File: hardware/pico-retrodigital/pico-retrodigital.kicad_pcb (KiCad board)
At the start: 2 copper layers, 53.8 x 35 mm, 44 parts, among them J1 Conn_02x05_Top_Bottom, J2 HDMI_A, J4 Conn_01x02_Pin, J5 USB_C, J5 USB_C_Plug_USB2.0, SW1 SW_Push, U6 74LVC2G17, U7 RP2350B, U8 NCP1117-3.3_SOT223, Y1 ABM8-272-T3

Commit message: PCB fixes
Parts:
- removed C4: 0.1u, Capacitor_SMD:C_0603_1608Metric
- removed J2: HDMI_A, Connector_Video:HDMI_A_Molex_208658-1001_Horizontal
- removed the J5 at (72.5, 107.2)
- removed the J5 at (73.8, 123.2)
- added C14: 4.7u, Capacitor_SMD:C_0402_1005Metric, F.Cu at (23.3, 120.6)
- added C15: 4.7u, Capacitor_SMD:C_0402_1005Metric, F.Cu at (23.3, 122.5)
- added J3: Conn_01x14, Connector_FFC-FPC:TE_1-1734839-4_1x14-1MP_P0.5mm_Horizontal, F.Cu at (95.3, 92.5)
- added J5: USB_C_Plug_USB2.0, pico-retrodigital:USB_C_Receptacle_Jing_918-418K2023S40001, F.Cu at (73.1, 105.1)
- added L1: 3.3u, Inductor_SMD:L_0805_2012Metric, F.Cu at (29.7, 120.6)
- U7: value RP2350B -> RP2354B; footprint rpi-lib-kicad-rp235x:QFN-80-1EP_10x10mm_P0.4mm_EP3.4x3.4mm_ThermalVias -> Package_DFN_QFN:QFN-80-1EP_10x10mm_P0.4mm_EP3.4x3.4mm_ThermalVias
- moved C13 47.2 mm to (23.3, 118.6)
- moved R15 46.9 mm to (37.5, 119.0)
- moved R14 38.5 mm to (37.5, 117.0), turned to 0 degrees
- moved R13 36.8 mm to (37.5, 115.0), turned to 0 degrees
- moved SW1 31.9 mm to (25.2, 91.9)
- moved R11 22.5 mm to (37.5, 113.0)
- moved D3 19.7 mm to (35.5, 109.5)
- moved D1 10.9 mm to (29.5, 123.2)
- moved J4 10.7 mm to (29.7, 114.3), turned to 0 degrees
- moved R16 9.94 mm to (34.0, 118.3)
- moved R17 9.94 mm to (34.0, 120.8)
- moved R18 9.94 mm to (34.0, 123.3)
- moved C7 7.95 mm to (23.7, 114.8), turned to 0 degrees
- moved F1 4.08 mm to (34.0, 113.3), turned to 0 degrees
- moved FB1 1.22 mm to (34.0, 115.8)
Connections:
- C12 pad 1: VBUS -> 5V
- D3 pad 1: VBUS -> 5V
- U7 pad 10: Net-(U7-DVDD-Pad10) -> unconnected-(U7-DVDD-Pad10)
- U7 pad 15: Net-(U7-IOVDD-Pad15) -> unconnected-(U7-IOVDD-Pad15)_6
- U7 pad 20: unconnected-(U7-GPIO20-Pad20) -> SDA
- U7 pad 21: unconnected-(U7-GPIO21-Pad21) -> SCL
- U7 pad 22: CTL_0 -> CEC_PICO
- U7 pad 23: CTL_1 -> unconnected-(U7-GPIO23-Pad23)
- U7 pad 24: Net-(U7-IOVDD-Pad15) -> unconnected-(U7-IOVDD-Pad15)_7
- U7 pad 25: CTL_2 -> CTL_0
- U7 pad 26: CTL_3 -> CTL_1
- U7 pad 27: CTL_4 -> CTL_2
- U7 pad 28: CTL_5 -> CTL_3
- U7 pad 29: Net-(U7-IOVDD-Pad15) -> unconnected-(U7-IOVDD-Pad15)
- U7 pad 32: Net-(U7-DVDD-Pad10) -> unconnected-(U7-DVDD-Pad10)_2
- U7 pad 41: Net-(U7-IOVDD-Pad15) -> unconnected-(U7-IOVDD-Pad15)_1
- U7 pad 5: Net-(U7-IOVDD-Pad15) -> unconnected-(U7-IOVDD-Pad15)_2
- U7 pad 50: Net-(U7-IOVDD-Pad15) -> unconnected-(U7-IOVDD-Pad15)_4
- U7 pad 51: Net-(U7-DVDD-Pad10) -> unconnected-(U7-DVDD-Pad10)_1
- U7 pad 60: Net-(U7-IOVDD-Pad15) -> unconnected-(U7-IOVDD-Pad15)_3
- U7 pad 76: Net-(U7-IOVDD-Pad15) -> unconnected-(U7-IOVDD-Pad15)_5
- U7 pad 77: unconnected-(U7-GPIO0-Pad77) -> AUD_DAT
- U7 pad 78: unconnected-(U7-GPIO1-Pad78) -> AUD_WS
- U7 pad 79: unconnected-(U7-GPIO2-Pad79) -> AUD_CLK
- U7 pad 8: unconnected-(U7-GPIO10-Pad8) -> AUX_A
- U7 pad 9: unconnected-(U7-GPIO11-Pad9) -> AUX_B
- U8 pad 3: VBUS -> 5V
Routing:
- net 5V: track 11.1 -> 0.00 mm
- net USB_D-: track 3.73 -> 0.00 mm
- net USB_D+: track 3.72 -> 0.00 mm
- net Net-(F1-Pad1): track 1.61 -> 0.00 mm
- net Net-(D1-K): track 1.61 -> 0.00 mm

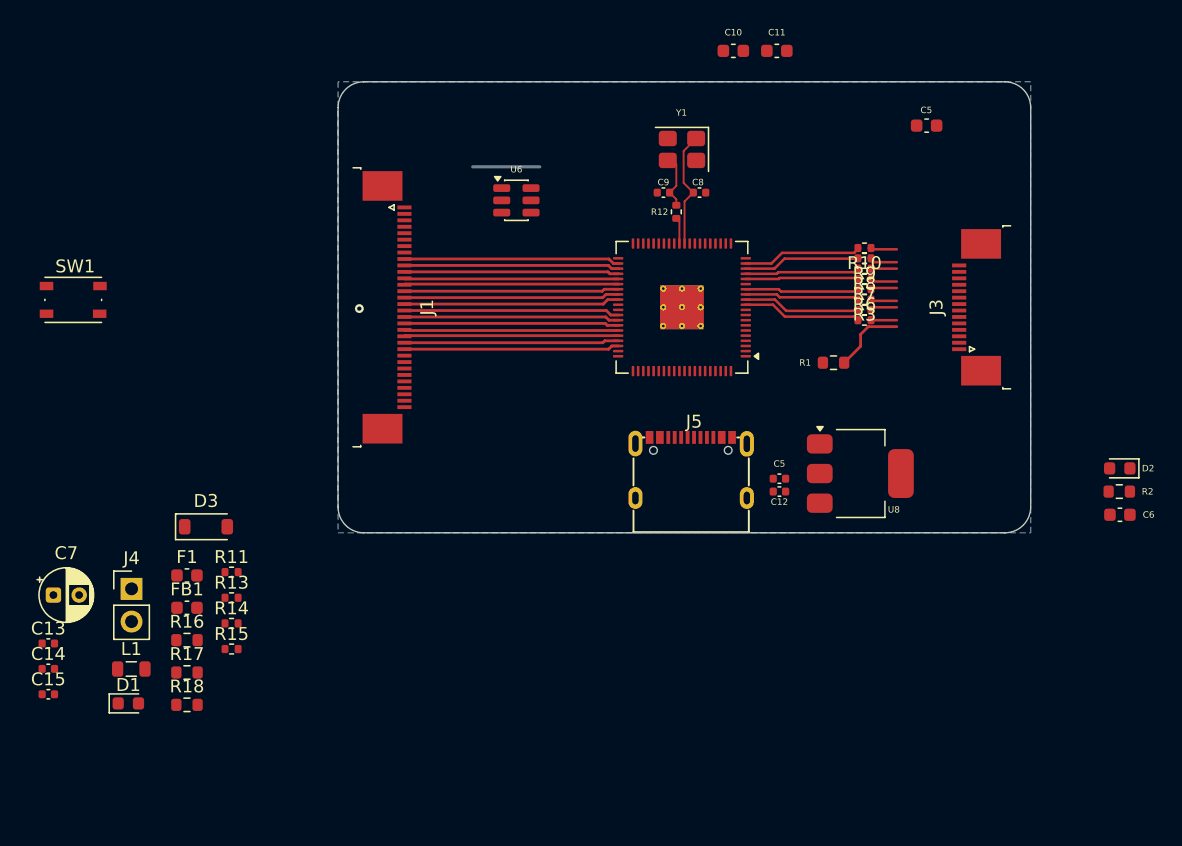
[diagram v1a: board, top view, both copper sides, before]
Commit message: Square-shaped PCB
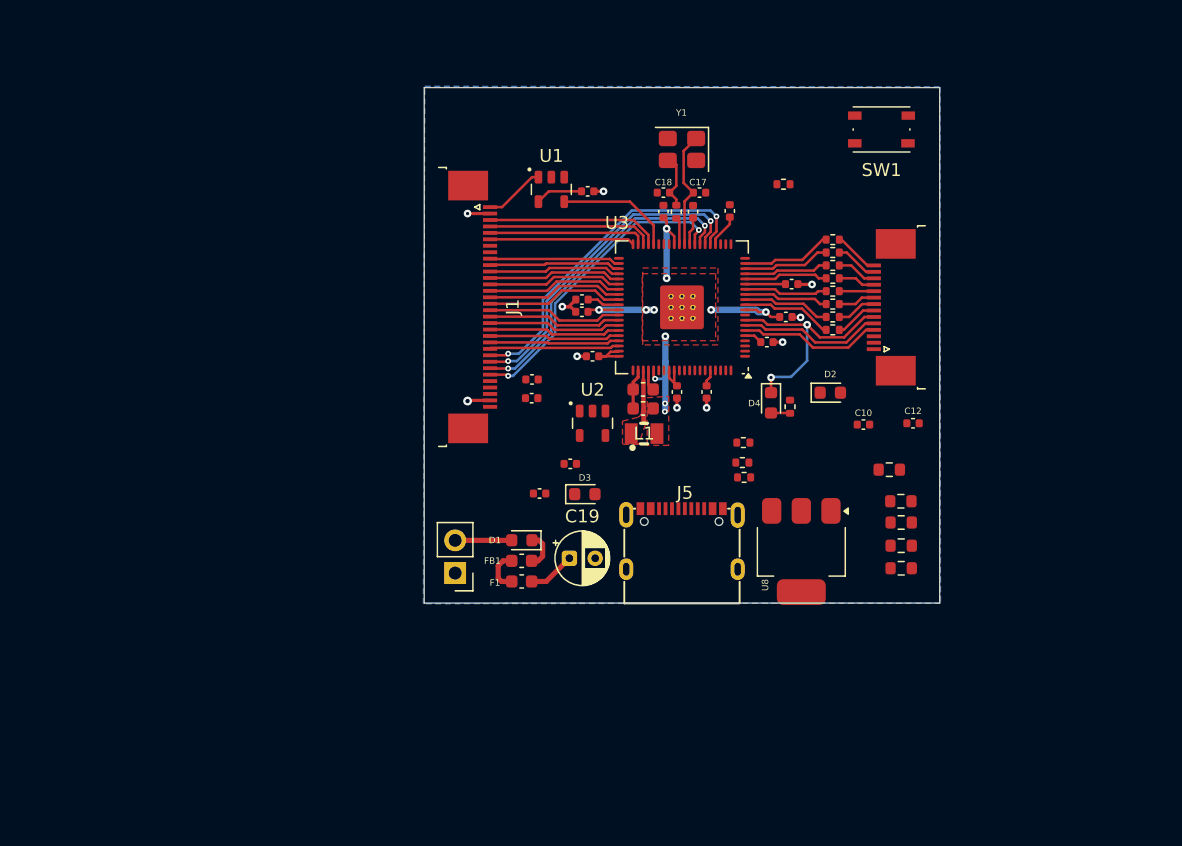
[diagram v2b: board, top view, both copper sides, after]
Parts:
- removed the C10 at (76.4, 72.6)
- removed the C5 at (91.4, 78.4)
- removed U6: 74LVC2G17, Package_TO_SOT_SMD:SOT-23-6
- added C1: 0.1u, Capacitor_SMD:C_0402_1005Metric, F.Cu at (81.0, 90.7)
- added C16: 0.1u, Capacitor_SMD:C_0402_1005Metric, F.Cu at (65.1, 83.5)
- added C19: 47u, Capacitor_THT:CP_Radial_D4.0mm_P2.00mm, F.Cu at (63.7, 112.0)
- added C2: 0.1u, Capacitor_SMD:C_0603_1608Metric, F.Cu at (69.4, 98.9)
- added C20: 0.1u, Capacitor_SMD:C_0402_1005Metric, F.Cu at (64.7, 92.8)
- added C21: 0.1u, Capacitor_SMD:C_0402_1005Metric, F.Cu at (71.0, 85.1)
- added C22: 0.1u, Capacitor_SMD:C_0402_1005Metric, F.Cu at (80.5, 93.2)
- added C3: 0.1u, Capacitor_SMD:C_0402_1005Metric, F.Cu at (64.7, 91.9)
- added C4: 0.1u, Capacitor_SMD:C_0402_1005Metric, F.Cu at (65.5, 96.3)
- added C5: 0.1u, Capacitor_SMD:C_0402_1005Metric, F.Cu at (76.2, 85.0)
- added C5: 0.1u, Capacitor_SMD:C_0402_1005Metric, F.Cu at (73.3, 85.1)
- added C8: 0.1u, Capacitor_SMD:C_0402_1005Metric, F.Cu at (72.0, 99.1)
- added C9: 0.1u, Capacitor_SMD:C_0402_1005Metric, F.Cu at (60.8, 98.1)
- added D4: SS14, Diode_SMD:D_0603_1608Metric, F.Cu at (79.3, 99.9)
- added R19: 5.1k, Resistor_SMD:R_0603_1608Metric, F.Cu at (89.5, 112.8)
- added U1: SN74LVC1G17DBVR, pico-retrodigital:SOT-23-5, F.Cu at (62.3, 83.3)
- added U2: SN74LVC1G17DBVR, pico-retrodigital:SOT-23-5, F.Cu at (65.5, 101.5)
- C11, C6: footprint Capacitor_SMD:C_0603_1608Metric -> Capacitor_SMD:C_0402_1005Metric
- C14: footprint Capacitor_SMD:C_0402_1005Metric -> Capacitor_SMD:C_0603_1608Metric
- C7: value 47u -> 0.1u; footprint Capacitor_THT:CP_Radial_D4.0mm_P2.00mm -> Capacitor_SMD:C_0402_1005Metric
- D3: value D_Schottky -> SS14; footprint Diode_SMD:D_SOD-123 -> Diode_SMD:D_0603_1608Metric
- L1: value 3.3u -> ~; footprint Inductor_SMD:L_0805_2012Metric -> pico-retrodigital:IND-SMD_L2.0-W1.6_AOTA-B201610S3R3-101-T
- R1: footprint Resistor_SMD:R_0603_1608Metric -> Resistor_SMD:R_0402_1005Metric
- U3: renamed from U7; footprint Package_DFN_QFN:QFN-80-1EP_10x10mm_P0.4mm_EP3.4x3.4mm_ThermalVias -> rpi-lib-kicad-rp235x:QFN-80-1EP_10x10mm_P0.4mm_EP3.4x3.4mm_ThermalVias
- moved SW1 64.1 mm to (87.9, 78.7)
- moved R18 56.8 mm to (89.5, 111.0)
- moved R17 56.6 mm to (89.5, 109.2)
- moved R16 56.4 mm to (89.4, 107.5)
- moved C7 53.1 mm to (74.3, 99.1), turned to -90 degrees
- moved R11 52.3 mm to (80.3, 83.0)
- moved C14 50.4 mm to (69.4, 100.3)
- moved L1 43.8 mm to (69.5, 102.3), turned to 180 degrees
- moved C13 42.1 mm to (60.8, 99.5)
- moved R15 41.9 mm to (77.3, 105.7)
- moved R14 41.6 mm to (77.1, 104.5)
- moved R13 41.5 mm to (77.2, 103.0)
- moved C15 41.2 mm to (61.4, 107.0)
- moved C11 35.8 mm to (63.8, 104.7), turned to 180 degrees
- moved D1 33.1 mm to (60.0, 110.6), turned to 180 degrees
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- renumbered C5 to C10, C8 to C17, C9 to C18
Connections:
- C11 pad 1: 3V3 -> +3V3
- C12 pad 1: 5V -> +5V
- C6 pad 1: Net-(D2-K) -> +3V3
- C7 pad 1: 5V -> +3V3
- D1 pad 2: 5V -> +5V
- D2 pad 2: 5V -> +5V
- D3 pad 1: 5V -> +5V
- F1 pad 2: 5V -> +5V
- J4 pad 2: 5V -> +5V
- J5 pad B5: Net-(J5-CC1) -> Net-(J5-CC2)
- R1 pad 2: CEC_PICO -> Net-(D4-A)
- R2 pad 1: 5V -> +5V
- U3 pad 10: unconnected-(U7-DVDD-Pad10) -> +1V1
- U3 pad 15: unconnected-(U7-IOVDD-Pad15)_6 -> +3V3
- U3 pad 20: SDA -> AUX_B
- U3 pad 21: SCL -> AUX_A
- U3 pad 22: CEC_PICO -> unconnected-(U3-GPIO22-Pad22)
- U3 pad 24: unconnected-(U7-IOVDD-Pad15)_7 -> +3V3
- U3 pad 29: unconnected-(U7-IOVDD-Pad15) -> +3V3
- U3 pad 32: unconnected-(U7-DVDD-Pad10)_2 -> +1V1
- U3 pad 41: unconnected-(U7-IOVDD-Pad15)_1 -> +3V3
- U3 pad 5: unconnected-(U7-IOVDD-Pad15)_2 -> +3V3
- U3 pad 50: unconnected-(U7-IOVDD-Pad15)_4 -> +3V3
- U3 pad 51: unconnected-(U7-DVDD-Pad10)_1 -> +1V1
- U3 pad 59: unconnected-(U7-ADC_AVDD-Pad59) -> +3V3
- U3 pad 6: unconnected-(U7-GPIO8-Pad6) -> SDA
- U3 pad 60: unconnected-(U7-IOVDD-Pad15)_3 -> +3V3
- U3 pad 68: unconnected-(U7-USB_OTP_VDD-Pad68) -> +3V3
- U3 pad 69: unconnected-(U7-QSPI_IOVDD-Pad69) -> +3V3
- U3 pad 7: unconnected-(U7-GPIO9-Pad7) -> SCL
- U3 pad 76: unconnected-(U7-IOVDD-Pad15)_5 -> +3V3
- U3 pad 8: AUX_A -> CEC_PICO
- U3 pad 9: AUX_B -> unconnected-(U3-GPIO11-Pad9)
- U8 pad 3: 5V -> +5V
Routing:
- net +1V1: track 0.00 -> 28.8 mm, vias 0 -> 11
- net CTL_0: track 0.00 -> 26.1 mm, vias 0 -> 2
- net CTL_1: track 0.00 -> 25.4 mm, vias 0 -> 2
- net CTL_2: track 0.00 -> 24.7 mm, vias 0 -> 2
- net +3V3: track 0.00 -> 24.3 mm
- net CTL_3: track 0.00 -> 23.8 mm, vias 0 -> 2
- net CMOD_0: track 0.00 -> 13.5 mm
- net CMOD_1: track 0.00 -> 12.9 mm
- net CEC_PICO: track 5.79 -> 18.5 mm, vias 0 -> 2
- net CMOD_2: track 0.00 -> 12.2 mm
- net CMOD_3: track 0.00 -> 11.2 mm
- net SCL: track 0.00 -> 11.2 mm
- net SDA: track 0.00 -> 11.1 mm
- net GND: track 5.20 -> 14.6 mm, vias 1 -> 10
- net PCLK: track 0.00 -> 9.16 mm
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- added copper zone on F.Cu, net +1V1
- added copper zone on F.Cu, net Net-(U3-VREG_LX)
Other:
- board size 53.8 x 35 mm -> 40 x 40 mm

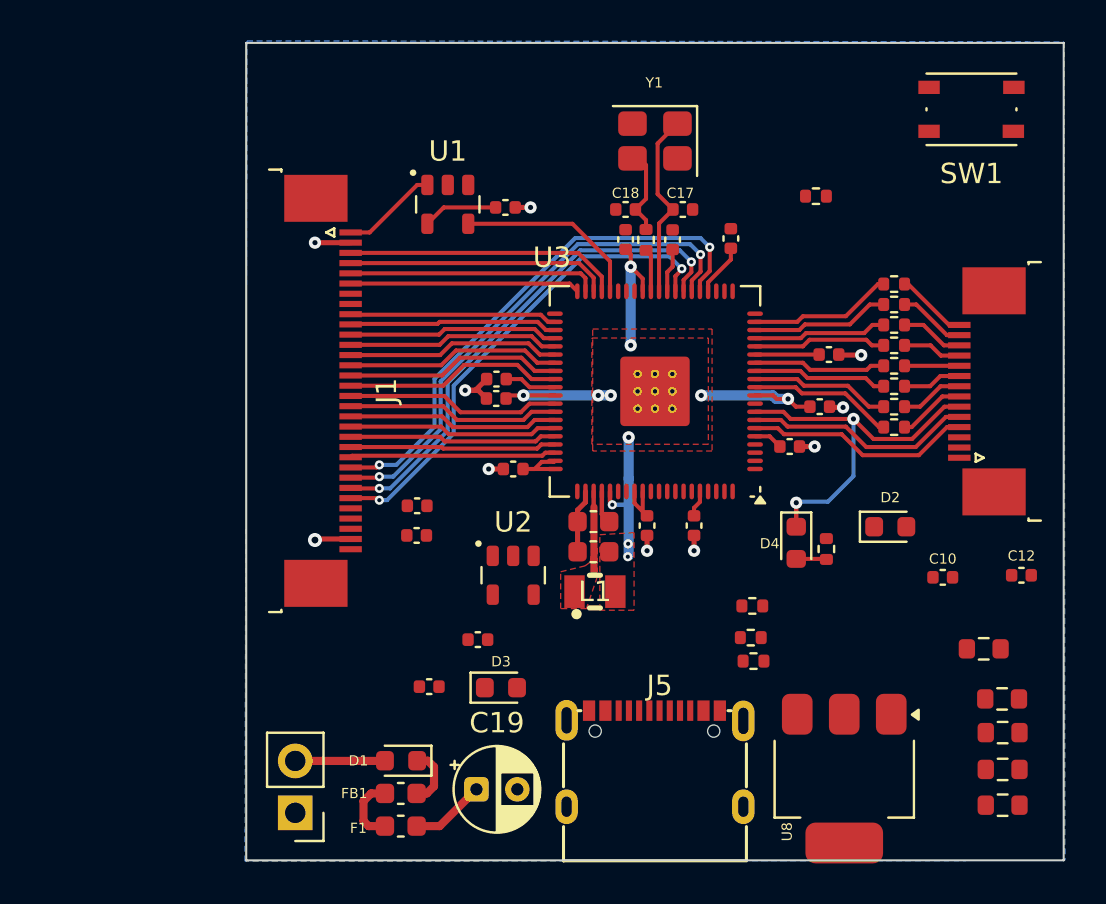
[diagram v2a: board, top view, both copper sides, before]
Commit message: Add 3V3 LDO regulator, reset/boot buttons, and pad default tweaks
- Add ME6217C33M5G LDO symbol and integrate into schematic
- Add RES1 (reset) and BOOT1 (boot) push buttons
- Update default pad size in board setup
- Ignore kicad-jlcpcb-tools plugin local state (jlcpcb/)
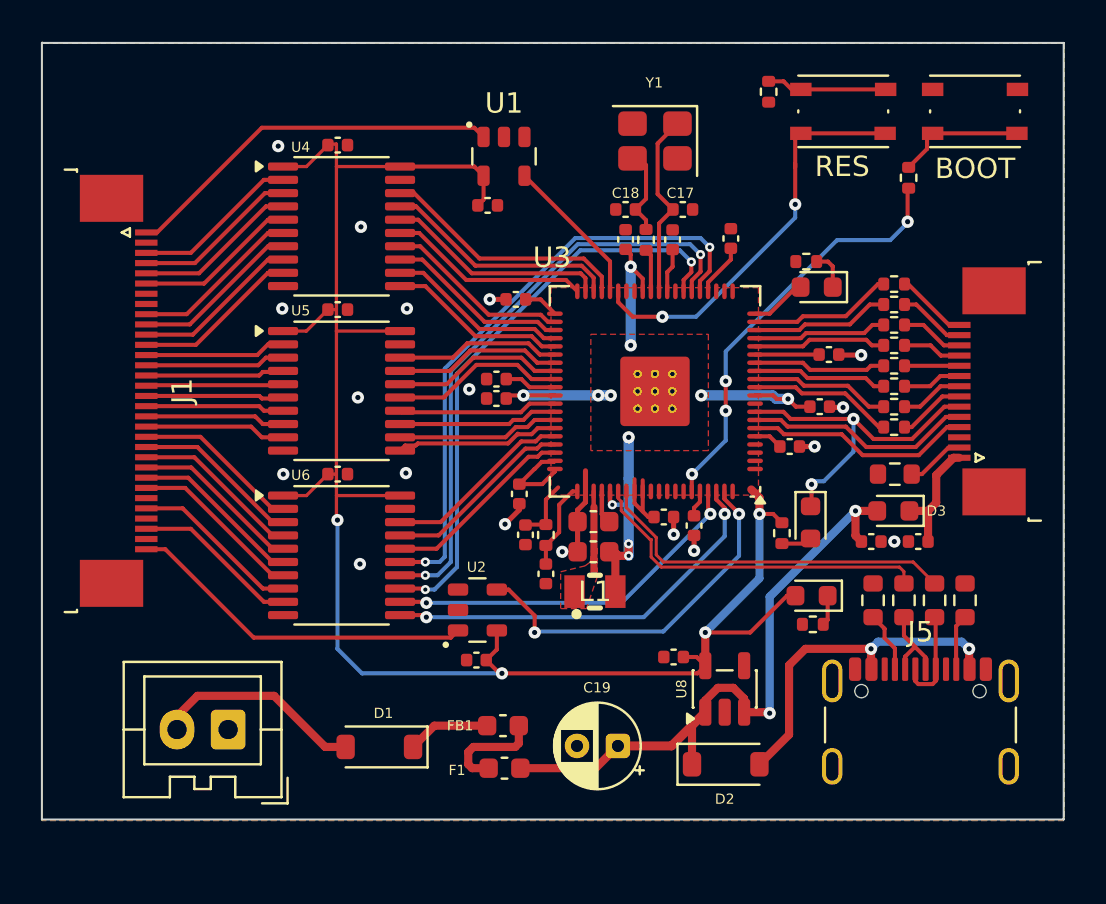
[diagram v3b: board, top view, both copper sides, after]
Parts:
- removed the D3 at (64.9, 107.0)
- added C24: 0.1u, Capacitor_SMD:C_0402_1005Metric, F.Cu at (56.9, 80.5)
- added C25: 0.1u, Capacitor_SMD:C_0402_1005Metric, F.Cu at (56.9, 88.5)
- added C26: 0.1u, Capacitor_SMD:C_0402_1005Metric, F.Cu at (56.9, 96.5)
- added C9: 0.1u, Capacitor_SMD:C_0402_1005Metric, F.Cu at (65.6, 88.0)
- added D2: D_Schottky, Diode_SMD:D_SOD-123, F.Cu at (75.9, 110.8)
- added D5: LED, LED_SMD:LED_0603_1608Metric, F.Cu at (80.1, 102.5)
- added D6: LED, LED_SMD:LED_0603_1608Metric, F.Cu at (80.3, 87.4)
- added R20: 2K, Resistor_SMD:R_0402_1005Metric, F.Cu at (79.8, 86.2)
- added RES: RES, Button_Switch_SMD:SW_Push_1P1T_NO_Vertical_Wuerth_434133025816, F.Cu at (81.7, 78.8)
- added U4: SN74LVC245APW, Package_SO:TSSOP-20_4.4x6.5mm_P0.65mm, F.Cu at (57.1, 84.4)
- added U5: SN74LVC245APW, Package_SO:TSSOP-20_4.4x6.5mm_P0.65mm, F.Cu at (57.1, 92.5)
- added U6: SN74LVC245APW, Package_SO:TSSOP-20_4.4x6.5mm_P0.65mm, F.Cu at (57.1, 100.5)
- BOOT: renamed from SW1; value SW_Push -> BOOT
- D1: value SS14 -> D_Schottky; footprint Diode_SMD:D_0603_1608Metric -> Diode_SMD:D_SOD-123
- J4: footprint Connector_PinHeader_2.54mm:PinHeader_1x02_P2.54mm_Vertical -> Connector_JST:JST_XA_B02B-XASK-1_1x02_P2.50mm_Vertical
- J5: footprint pico-retrodigital:USB_C_Receptacle_Jing_918-418K2023S40001 -> Connector_USB:USB_C_Receptacle_GCT_USB4105-xx-A_16P_TopMnt_Horizontal
- R13: value 27 -> 1k
- R14: value 27 -> 2K
- U8: value NCP1117-3.3_SOT223 -> ME6217C33M5G; footprint Package_TO_SOT_SMD:SOT-223-3_TabPin2 -> Package_TO_SOT_SMD:SOT-23-5
- moved R13 25.2 mm to (78.0, 77.8), turned to 90 degrees
- moved C23 24.6 mm to (85.3, 99.8), turned to 180 degrees
- moved C10 13.7 mm to (73.3, 105.5), turned to 180 degrees
- moved J5 13.0 mm to (85.4, 109.8)
- moved R15 11.9 mm to (67.1, 99.5), turned to 90 degrees
- moved R18 10.4 mm to (83.1, 102.7), turned to -90 degrees
- moved R19 10.2 mm to (87.6, 102.7), turned to 90 degrees
- moved J1 10.0 mm to (46.2, 92.5)
- moved R2 9.59 mm to (84.2, 96.5)
- moved C15 8.80 mm to (66.1, 99.5), turned to -90 degrees
- moved R17 8.08 mm to (84.6, 102.7), turned to -90 degrees
- moved C12 7.53 mm to (83.0, 99.8)
- moved U8 7.31 mm to (75.8, 107.1), turned to 90 degrees
- moved C19 7.24 mm to (70.6, 109.8), turned to 180 degrees
- moved C13 6.60 mm to (67.1, 101.4), turned to -90 degrees
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- renumbered C9 to C23, D2 to D3
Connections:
- D1 pad 2: +5V -> +5V MVS
- J1 pad 10: R1 -> IN_R1
- J1 pad 11: R2 -> IN_R2
- J1 pad 12: R3 -> IN_R3
- J1 pad 13: R4 -> IN_R4
- J1 pad 14: G0 -> IN_G0
- J1 pad 15: G1 -> IN_G1
- J1 pad 16: G2 -> IN_G2
- J1 pad 17: G3 -> IN_G3
- J1 pad 18: G4 -> IN_G4
- J1 pad 19: B0 -> IN_B0
- J1 pad 20: B1 -> IN_B1
- J1 pad 21: B2 -> IN_B2
- J1 pad 22: B3 -> IN_B3
- J1 pad 23: B4 -> IN_B4
- J1 pad 24: CTL_0 -> IN_CTL_0
- J1 pad 25: CTL_1 -> IN_CTL_1
- J1 pad 26: CTL_2 -> IN_CTL_2
- J1 pad 27: CTL_3 -> unconnected-(J1-Pin_27-Pad27)
- J1 pad 28: AUD_WS -> IN_AUD_DAT
- J1 pad 3: CMOD_0 -> IN_CMOD_0
- J1 pad 30: AUD_DAT -> IN_AUD_WS
- J1 pad 4: CMOD_1 -> IN_CMOD_1
- J1 pad 5: CMOD_2 -> IN_CMOD_2
- J1 pad 6: CMOD_3 -> IN_CMOD_3
- J1 pad 7: AUX_A -> unconnected-(J1-Pin_7-Pad7)
- J1 pad 8: AUX_B -> unconnected-(J1-Pin_8-Pad8)
- J1 pad 9: R0 -> IN_R0
- J4 pad 2: +5V -> +5V MVS
- R13 pad 1: USB_D- -> GND
- R13 pad 2: Net-(U3-USB_DM) -> Net-(R13-Pad2)
- R14 pad 1: USB_D+ -> Net-(D5-K)
- R14 pad 2: Net-(U3-USB_DP) -> GND
- U3 pad 20: AUX_B -> Net-(D6-A)
- U3 pad 21: AUX_A -> unconnected-(U3-GPIO21-Pad21)
- U3 pad 28: CTL_3 -> unconnected-(U3-GPIO27-Pad28)
- U3 pad 35: unconnected-(U3-RUN-Pad35) -> Net-(U3-RUN)
- U3 pad 66: Net-(U3-USB_DM) -> USB_D-
- U3 pad 67: Net-(U3-USB_DP) -> USB_D+
- U8 pad 1: GND -> +5V
- U8 pad 2: +3V3 -> GND
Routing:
- net +3V3: track 24.3 -> 115.8 mm, vias 0 -> 4
- net +5V: track 8.07 -> 32.2 mm, vias 0 -> 2
- net CTL_3: track 23.8 -> 0.00 mm, vias 2 -> 0
- net Net-(U3-QSPI_SS): track 0.00 -> 20.8 mm, vias 0 -> 4
- net Net-(U3-RUN): track 0.00 -> 20.1 mm, vias 0 -> 2
- net AUD_WS: track 0.00 -> 19.9 mm, vias 0 -> 2
- net AUD_CLK: track 0.00 -> 18.2 mm, vias 0 -> 2
- net AUD_DAT: track 0.00 -> 18.2 mm, vias 0 -> 2
- net USB_D+: track 0.00 -> 17.9 mm
- net IN_AUD_CLK: track 0.00 -> 17.2 mm
- net USB_D-: track 0.00 -> 17.1 mm
- net Net-(D2-A): track 0.00 -> 16.9 mm, vias 0 -> 2
- net IN_PCLK: track 4.72 -> 18.8 mm
- net +5V MVS: track 0.00 -> 10.3 mm
- net IN_CTL_2: track 0.00 -> 8.46 mm
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- added copper zone on F.Cu, net +3V3
- added copper zone on F.Cu, net GND
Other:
- board size 40 x 40 mm -> 50 x 38 mm
